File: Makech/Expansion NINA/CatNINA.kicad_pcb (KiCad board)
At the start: 2 copper layers, 62.9 x 33.4 mm, 25 parts, among them J1 Conn_02x03_Odd_Even, J2 Conn_02x03_Odd_Even, P3 PROGRAMMER SERIAL, P4 Battery, U1 ESP32-WROOM, U2 AP2112K-3.3TRG1, U3 MCP73831T-2ACI/OT

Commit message: Init PCB and netlist
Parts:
- removed C2, C3, C4: 10uF, Capacitors_SMD:C_0805_HandSoldering
- removed D2: D_Schottky, Diodes_SMD:D_SOD-123F
- removed D3: LED, LEDs:LED_0805_HandSoldering
- removed J2: Conn_02x03_Odd_Even, Pines:62000621121
- removed P3: PROGRAMMER SERIAL, Pin_Headers:Pin_Header_Straight_1x06_Pitch2.54mm
- removed P4: Battery, Pin_Headers:Pin_Header_Straight_1x02_Pitch2.54mm
- removed R4, R5: 10k, Resistors_SMD:R_0805_HandSoldering
- removed R6: 1K, Resistors_SMD:R_0805_HandSoldering
- removed R7: 4.7K, Resistors_SMD:R_0805_HandSoldering
- removed R8: 10K, Resistors_SMD:R_0805_HandSoldering
- removed U2: AP2112K-3.3TRG1, TO_SOT_Packages_SMD:SOT-23-5_HandSoldering
- removed U3: MCP73831T-2ACI/OT, TO_SOT_Packages_SMD:SOT-23-5_HandSoldering
- G***: moved to B.Cu
- J1: value Conn_02x03_Odd_Even -> Expansion; footprint Pines:62000621121 -> Pines:61301221121
- R1: value 100k -> 330
- R2: value 100k -> 10k
- R3: value 330 -> 10K
- moved J1 46.0 mm to (193.8, 106.4), turned to 0 degrees
- moved C1 35.2 mm to (206.2, 86.9), turned to 90 degrees
- moved R3 22.1 mm to (206.0, 93.5), turned to 90 degrees
- moved G*** 15.8 mm to (190.4, 92.2), turned to 0 degrees
- moved R1 15.3 mm to (181.8, 105.5), turned to 180 degrees
- moved R2 11.9 mm to (180.5, 86.7)
- moved U1 6.52 mm to (193.9, 88.1)
- moved G*** 6.16 mm to (201.6, 87.3)
- moved D1 2.42 mm to (181.8, 108.1), turned to 180 degrees
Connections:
- J1 pad 1: /MOSI -> /ESP_TX
- J1 pad 2: /MISO -> +3V3
- J1 pad 3: /SCK -> /ESP_RX
- J1 pad 4: /ESP_GPIO0 -> /ESP_BUSY
- J1 pad 5: /ESP_RESET -> /ESP_CS
- J1 pad 6: VCC -> /ESP_RTS
- R1 pad 1: +BATT -> /IO25
- R1 pad 2: /AN35_BAT -> Net-(D1-Pad2)
- R2 pad 1: /AN35_BAT -> /ESP_RESET
- R3 pad 1: /IO25 -> +3V3
- R3 pad 2: Net-(D1-Pad2) -> /ESP_CS
- U1 pad 13: /MOSI -> /ESP_MOSI
- U1 pad 30: /SCK -> /ESP_SCK
- U1 pad 37: /MISO -> /ESP_MISO
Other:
- board size 62.9 x 33.4 mm -> 30.7 x 33.4 mm
- board text added: "CatNINA"
- board text removed: "Backpack BLE"

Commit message: size in margin
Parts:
- removed the G*** at (195.7, 80.4)
- added G***: LOGO, Aesthetics:escornabot_8x8, B.Cu at (184.5, 94.9)
- G***: moved to F.Cu
- moved C1 25.2 mm to (182.1, 79.6), turned to 180 degrees
- moved G*** 20.0 mm to (205.0, 105.8)
- moved G*** 9.24 mm to (200.7, 96.5)
- moved R2 2.46 mm to (180.4, 84.2), turned to 90 degrees
- moved R3 2.19 mm to (206.4, 95.6)
- moved J1 0.62 mm to (193.6, 106.9)
- turned D1 to 0 degrees
- turned R1 to 0 degrees
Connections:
- J1 pad 10: /ESP_RESET -> /ESP_SCK
- J1 pad 11: GND -> /ESP_RESET
- J1 pad 2: +3V3 -> /ESP_RX
- J1 pad 3: /ESP_RX -> /ESP_CS
- J1 pad 4: /ESP_BUSY -> /ESP_GPIO0
- J1 pad 5: /ESP_CS -> /ESP_MOSI
- J1 pad 6: /ESP_RTS -> GND
- J1 pad 7: /ESP_GPIO0 -> +3V3
- J1 pad 8: /ESP_SCK -> /ESP_BUSY
- J1 pad 9: /ESP_MOSI -> /ESP_RTS
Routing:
- net +3V3: track 0.00 -> 67.9 mm, vias 0 -> 2
- net /ESP_RESET: track 0.00 -> 53.0 mm, vias 0 -> 2
- net /ESP_CS: track 0.00 -> 43.1 mm, vias 0 -> 1
- net /ESP_RX: track 0.00 -> 35.2 mm, vias 0 -> 2
- net /ESP_TX: track 0.00 -> 33.4 mm
- net /ESP_MISO: track 0.00 -> 30.3 mm, vias 0 -> 1
- net /ESP_RTS: track 0.00 -> 25.4 mm, vias 0 -> 2
- net /ESP_MOSI: track 0.00 -> 22.7 mm
- net /ESP_BUSY: track 0.00 -> 20.7 mm, vias 0 -> 1
- net /ESP_SCK: track 0.00 -> 17.2 mm, vias 0 -> 1
- net /ESP_GPIO0: track 0.00 -> 16.6 mm, vias 0 -> 2
- net /IO25: track 0.00 -> 14.0 mm
- net GND: track 0.00 -> 11.3 mm, vias 0 -> 2
- net Net-(D1-Pad2): track 0.00 -> 2.63 mm
- added copper zone on B.Cu, net GND
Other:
- board text added: "Co-Processor"
- board text added: "ESP32 WIFI & BLE"
- board text added: "Escornabot Makech"
- board text added: "SPI Interface"
- board text added: "v0.1"

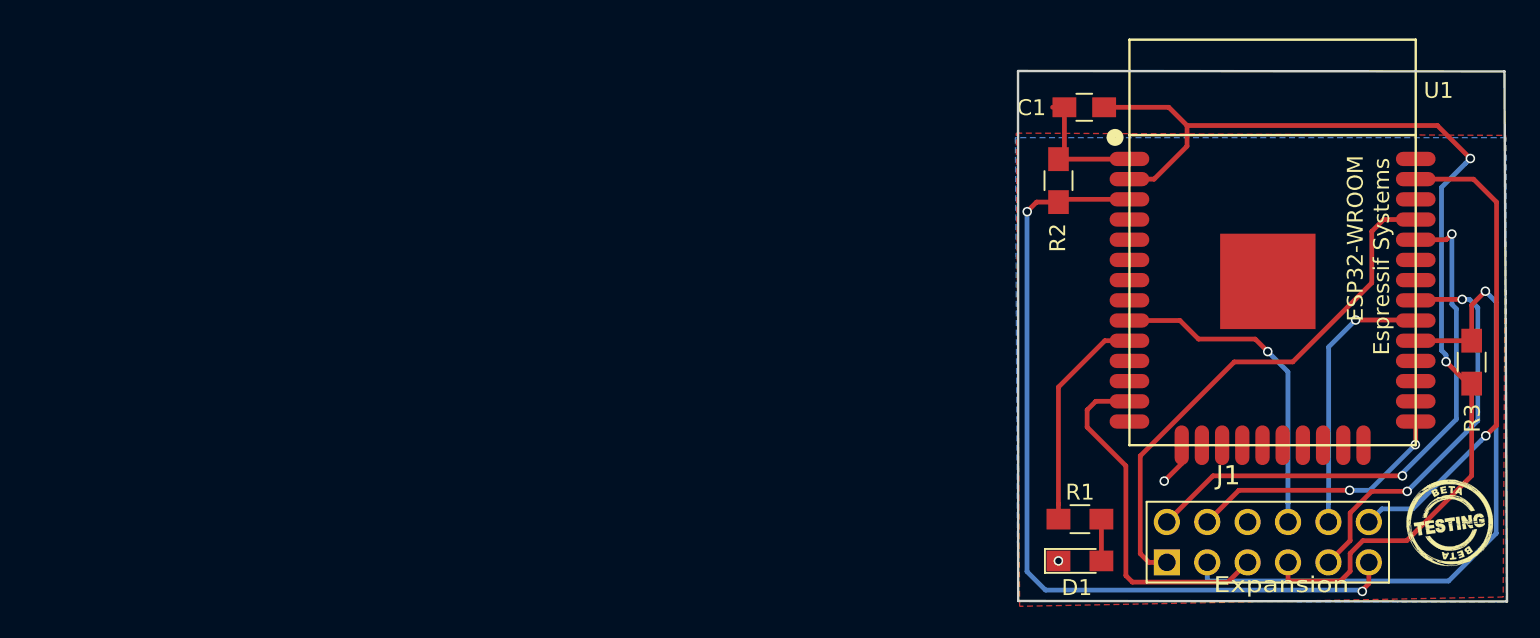
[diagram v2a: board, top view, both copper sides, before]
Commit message: routeo NINA
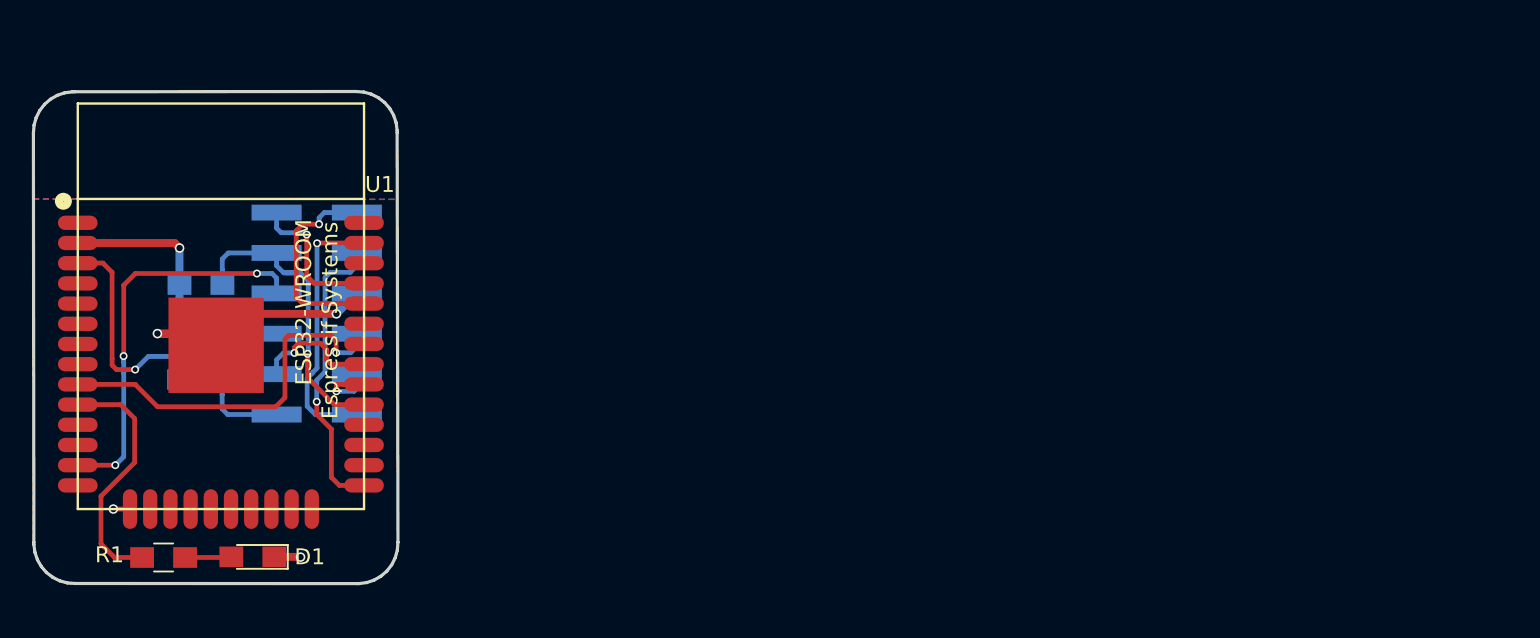
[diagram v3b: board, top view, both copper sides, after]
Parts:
- C1, G***, R2, R3: moved to B.Cu
- J1: value Expansion -> ESP; footprint Pines:61301221121 -> Connector_PinHeader_2.54mm:PinHeader_2x06_P2.54mm_Vertical_SMD; moved to B.Cu
- moved G*** 144.9 mm to (73.9, 44.1), turned to 180 degrees
- moved G*** 123.0 mm to (84.1, 57.2)
- moved G*** 116.9 mm to (74.7, 54.8)
- moved R3 80.1 mm to (126.5, 90.7), turned to 0 degrees
- moved U1 66.3 mm to (127.8, 92.1)
- moved J1 61.5 mm to (133.8, 92.6), turned to 180 degrees
- moved R1 57.7 mm to (124.2, 107.9)
- moved C1 57.2 mm to (126.6, 93.8)
- moved R2 55.4 mm to (126.5, 96.7), turned to 180 degrees
- moved D1 52.0 mm to (129.8, 107.9), turned to 180 degrees
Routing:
- net +3V3: track 67.9 -> 17.6 mm, vias 2 -> 1
- net /ESP_RESET: track 53.0 -> 22.3 mm, vias 2 -> 1
- net /ESP_TX: track 33.4 -> 9.44 mm, vias 0 -> 1
- net /ESP_CS: track 43.1 -> 19.6 mm
- net /ESP_RX: track 35.2 -> 13.1 mm, vias 2 -> 1
- net /ESP_RTS: track 25.4 -> 7.96 mm, vias 2 -> 1
- net /ESP_MISO: track 30.3 -> 17.2 mm
- net /ESP_SCK: track 17.2 -> 4.39 mm
- net GND: track 11.3 -> 18.5 mm, vias 2 -> 4
- net /ESP_BUSY: track 20.7 -> 24.6 mm
- net /ESP_MOSI: track 22.7 -> 25.2 mm, vias 0 -> 3
- net /ESP_GPIO0: track 16.6 -> 18.5 mm, vias 2 -> 1
- net /IO25: track 14.0 -> 15.6 mm
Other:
- board size 30.7 x 33.4 mm -> 22.9 x 30.9 mm
- net class Default: via_dia 0.6 -> 0.5; via_drill 0.4 -> 0.3
- net class Source added: clearance 0.2, trace_width 0.5, via_dia 0.6, via_drill 0.4

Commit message: model 3D CatNiNA
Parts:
- G***: moved to F.Cu
- moved G*** 71.3 mm to (128.5, 90.0)
- moved G*** 69.8 mm to (134.0, 106.0)
- moved G*** 68.3 mm to (120.5, 105.5)
